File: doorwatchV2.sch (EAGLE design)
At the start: 36 parts, among them IC2 MAX3232CPE, K1 FINDER-43.61, Q1 IRLZ44Z, T1 BC847, T2 BC847, T3 BC847, X1 MKDSN1,5/2-5,08, X2 D-SUB9-H2M09RA, X3 MKDSN1,5/2-5,08

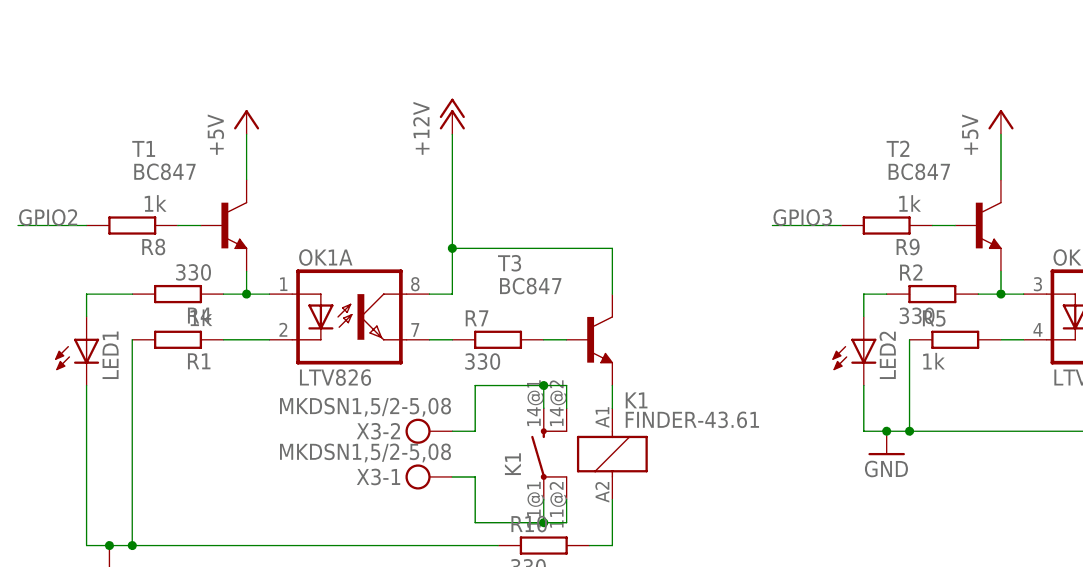
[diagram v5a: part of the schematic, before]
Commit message: changed the base resistors of the transistors to 10k
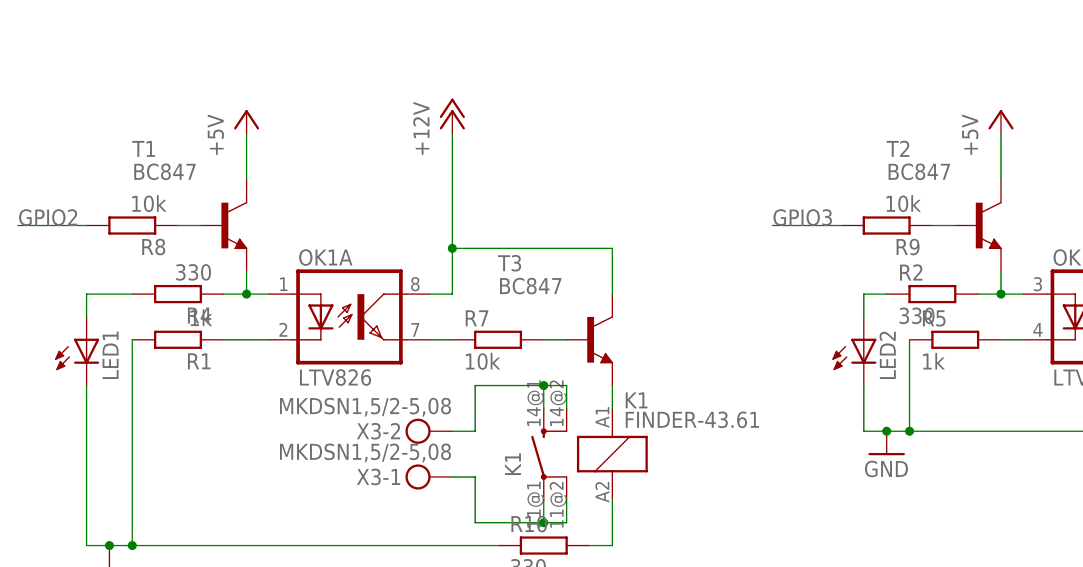
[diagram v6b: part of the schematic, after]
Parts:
- R7: value 330 -> 10k
- R8, R9: value 1k -> 10k
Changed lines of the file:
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@@
 <part name="R6" library="rcl" deviceset="R-EU_" device="M0805" value="330"/>
 <part name="K1" library="relay" deviceset="FINDER-43.61" device=""/>
-<part name="R7" library="rcl" deviceset="R-EU_" device="M0805" value="330"/>
+<part name="R7" library="rcl" deviceset="R-EU_" device="M0805" value="10k"/>
 <part name="P+7" library="supply1" deviceset="+12V" device=""/>
 <part name="X3" library="con-phoenix-508" deviceset="MKDSN1,5/2-5,08" device=""/>
-<part name="R8" library="rcl" deviceset="R-EU_" device="M0805" value="1k"/>
-<part name="R9" library="rcl" deviceset="R-EU_" device="M0805" value="1k"/>
+<part name="R8" library="rcl" deviceset="R-EU_" device="M0805" value="10k"/>
+<part name="R9" library="rcl" deviceset="R-EU_" device="M0805" value="10k"/>
 <part name="T3" library="transistor" deviceset="BC847" device=""/>
 <part name="R10" library="rcl" deviceset="R-EU_" device="M0805" value="330"/>

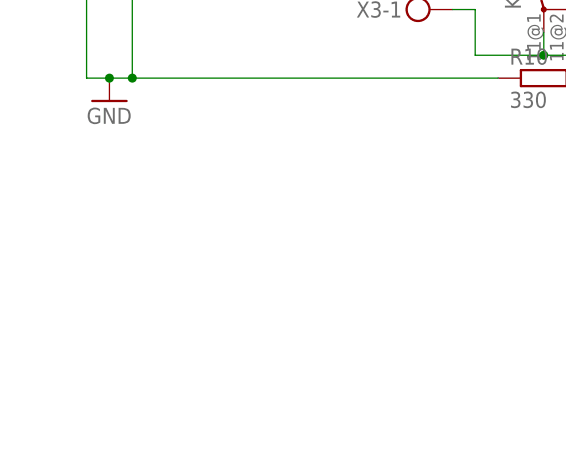
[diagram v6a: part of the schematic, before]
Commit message: added GPIO indication LED
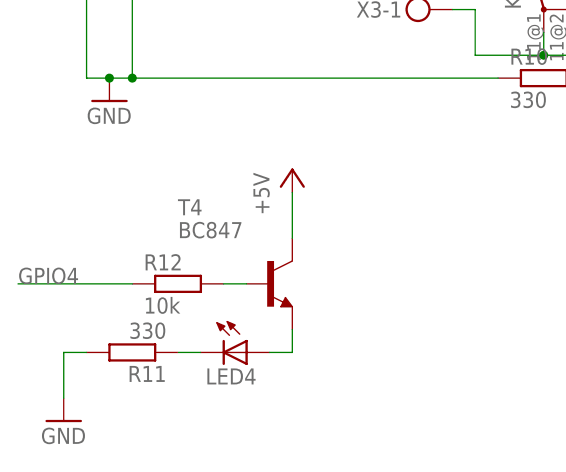
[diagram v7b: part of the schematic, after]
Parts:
- added LED4: (no value), led:LEDCHIP-LED0805
- added R11: 330, rcl:R-EU_M0805
- added R12: 10k, rcl:R-EU_M0805
- added T4: BC847, transistor:BC847
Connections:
- new net N$27: R12.2, T4.B
- new net N$28: LED4.A, T4.E
- new net N$29: LED4.C, R11.1
- net +5V: now also T4.C
- net GND: now also R11.2
- net GPIO4: now also R12.1
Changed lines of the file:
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@@
 <part name="T3" library="transistor" deviceset="BC847" device=""/>
 <part name="R10" library="rcl" deviceset="R-EU_" device="M0805" value="330"/>
+<part name="LED4" library="led" deviceset="LED" device="CHIP-LED0805"/>
+<part name="R11" library="rcl" deviceset="R-EU_" device="M0805" value="330"/>
+<part name="T4" library="transistor" deviceset="BC847" device=""/>
+<part name="R12" library="rcl" deviceset="R-EU_" device="M0805" value="10k"/>
+<part name="P+8" library="supply1" deviceset="+5V" device=""/>
+<part name="GND5" library="supply1" deviceset="GND" device=""/>
 </parts>
 <sheets>
@@
 <instance part="T3" gate="G$1" x="-20.32" y="-60.96"/>
 <instance part="R10" gate="G$1" x="-25.4" y="-83.82"/>
+<instance part="LED4" gate="G$1" x="-58.42" y="-114.3" rot="R270"/>
+<instance part="R11" gate="G$1" x="-71.12" y="-114.3" rot="R180"/>
+<instance part="T4" gate="G$1" x="-55.88" y="-106.68"/>
+<instance part="R12" gate="G$1" x="-66.04" y="-106.68"/>
+<instance part="P+8" gate="1" x="-53.34" y="-93.98"/>
+<instance part="GND5" gate="1" x="-78.74" y="-121.92"/>
 </instances>
 <busses>
@@
 <junction x="15.24" y="-71.12"/>
 </segment>
+<segment>
+<pinref part="R11" gate="G$1" pin="2"/>
+<wire x1="-76.2" y1="-114.3" x2="-78.74" y2="-114.3" width="0.1524" layer="91"/>
+<wire x1="-78.74" y1="-114.3" x2="-78.74" y2="-119.38" width="0.1524" layer="91"/>
+<pinref part="GND5" gate="1" pin="GND"/>
+</segment>
 </net>
 <net name="N$3" class="0">
@@
 <wire x1="25.4" y1="-38.1" x2="25.4" y2="-43.18" width="0.1524" layer="91"/>
 </segment>
+<segment>
+<pinref part="P+8" gate="1" pin="+5V"/>
+<pinref part="T4" gate="G$1" pin="C"/>
+<wire x1="-53.34" y1="-96.52" x2="-53.34" y2="-101.6" width="0.1524" layer="91"/>
+</segment>
 </net>
 <net name="+3V3" class="0">
@@
 <wire x1="-55.88" y1="15.24" x2="-71.12" y2="15.24" width="0.1524" layer="91"/>
 <label x="-71.12" y="15.24" size="1.778" layer="95"/>
+</segment>
+<segment>
+<pinref part="R12" gate="G$1" pin="1"/>
+<wire x1="-71.12" y1="-106.68" x2="-83.82" y2="-106.68" width="0.1524" layer="91"/>
+<label x="-83.82" y="-106.68" size="1.778" layer="95"/>
 </segment>
 </net>
@@
 </segment>
 </net>
+<net name="N$27" class="0">
+<segment>
+<pinref part="R12" gate="G$1" pin="2"/>
+<pinref part="T4" gate="G$1" pin="B"/>
+<wire x1="-60.96" y1="-106.68" x2="-58.42" y2="-106.68" width="0.1524" layer="91"/>
+</segment>
+</net>
+<net name="N$28" class="0">
+<segment>
+<pinref part="T4" gate="G$1" pin="E"/>
+<pinref part="LED4" gate="G$1" pin="A"/>
+<wire x1="-53.34" y1="-111.76" x2="-53.34" y2="-114.3" width="0.1524" layer="91"/>
+<wire x1="-53.34" y1="-114.3" x2="-55.88" y2="-114.3" width="0.1524" layer="91"/>
+</segment>
+</net>
+<net name="N$29" class="0">
+<segment>
+<pinref part="LED4" gate="G$1" pin="C"/>
+<pinref part="R11" gate="G$1" pin="1"/>
+<wire x1="-63.5" y1="-114.3" x2="-66.04" y2="-114.3" width="0.1524" layer="91"/>
+</segment>
+</net>

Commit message: splitted schematic parts to several sheets, updated descriptions, added info text. created board file (.brd)
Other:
- note added: "230V Relay"
- note added: "Indication LED"
- note added: "Opener"
- note added: "Power Supply"
- note added: "RPI Exp. Header"
- note added: "RS232 Interface"
